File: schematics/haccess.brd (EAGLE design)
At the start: 86 x 86 mm, 30 parts, among them IC1 MCP2300X/SO, Q2 BSS123, X2 MICROMATCH-6-SMD

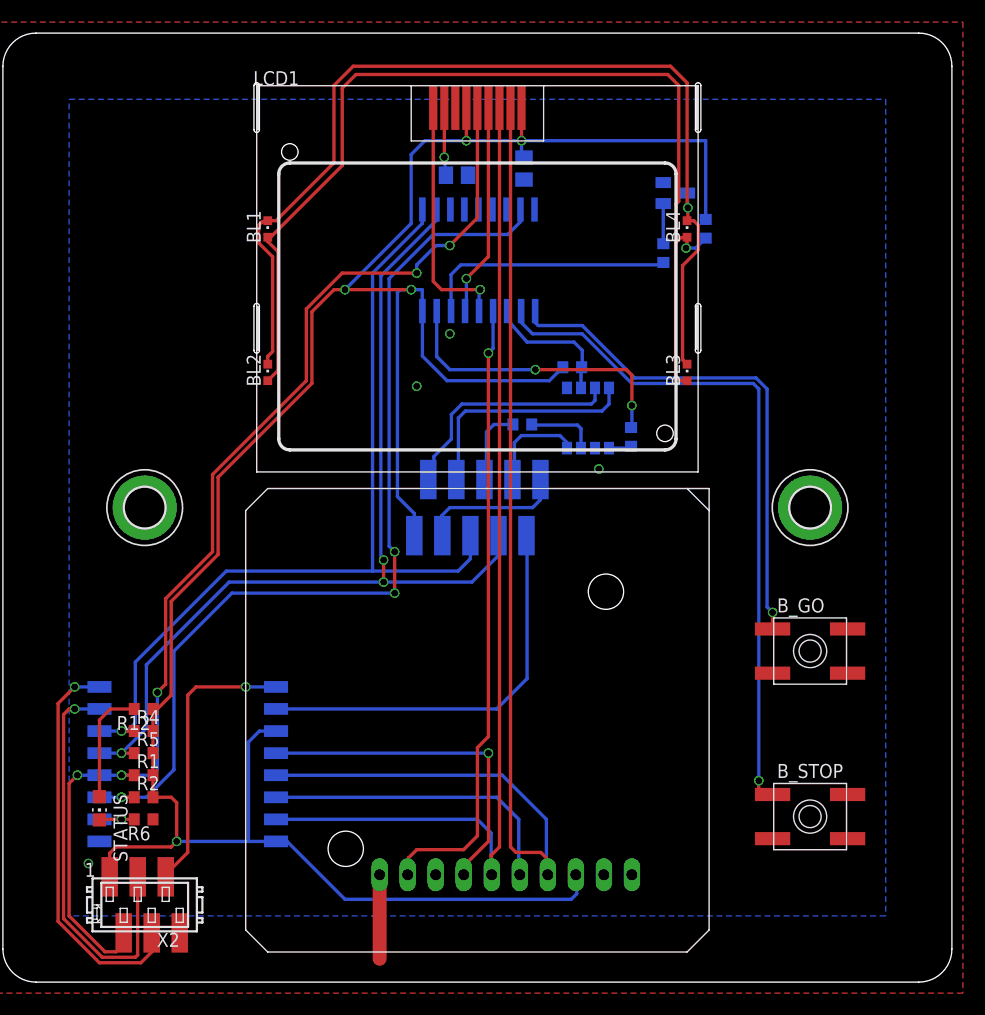
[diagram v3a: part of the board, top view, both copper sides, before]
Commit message: Added extra decoupling caps to ESP and MCP, added resistor to IRQ line, increased size of +3V3 lines, improved routing, fixed ground plane under ESP, changed switches to SKPMAPE010
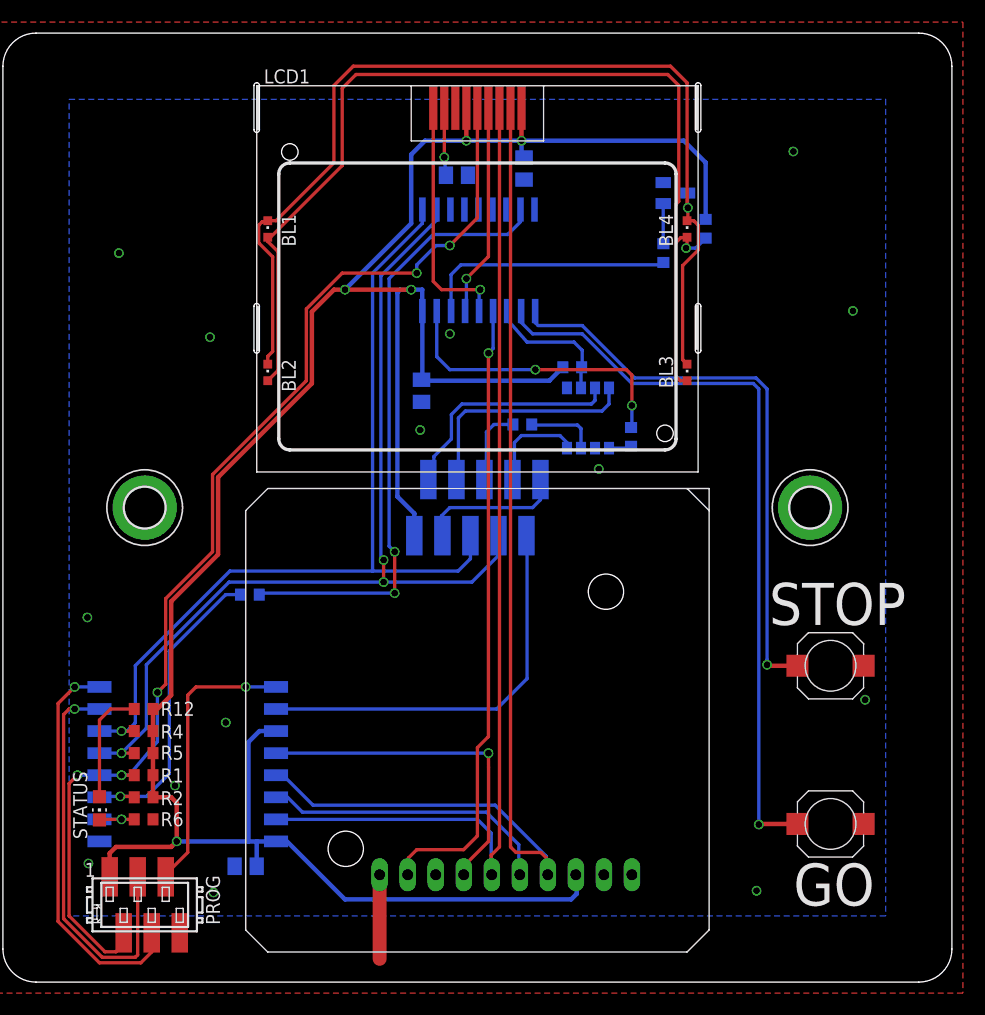
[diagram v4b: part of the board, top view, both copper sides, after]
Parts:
- removed B_GO, B_STOP: SPST_TACT-EVQQ2, adafruit:EVQ-Q2
- added C3, C4: 100nF, rcl:C0805K
- added R8: 22R, rcl:R0603
- added SW1, SW2: SPST_TACT, smtswitch:SKPMAPE010
- renumbered IC1 to U1, Q2 to Q1, U$2 to U2, U$3 to U3, X2 to PROG
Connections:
- new net !IRQ_1: R2.1, R8.2, U2.GPIO2
- net !IRQ: now also R8.1; no longer R2.1, U2.GPIO2
- net +3V3: now also C3.1, C4.1
- net GND: now also C3.2, C4.2, SW1.A, SW2.A; no longer B_GO.A, B_STOP.A
- net IN_G: now also SW2.B; no longer B_STOP.B
- net IN_R: now also SW1.B; no longer B_GO.B
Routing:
- net !IRQ: track 85.7 -> 56.2 mm, vias 3 -> 2
- net !IRQ_1: track 0.00 -> 28.2 mm, vias 0 -> 1
- net IN_R: track 46.5 -> 52.4 mm
- net IN_G: track 63.1 -> 68.1 mm
- net +3V3: track 228.7 -> 231.1 mm
- net SCK: track 103.4 -> 101.5 mm
- net MISO: track 27.9 -> 26.5 mm
- net CS0: track 105.9 -> 104.6 mm
- net GND: vias 4 -> 14
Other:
- board text added: "GO"
- board text added: "STOP"

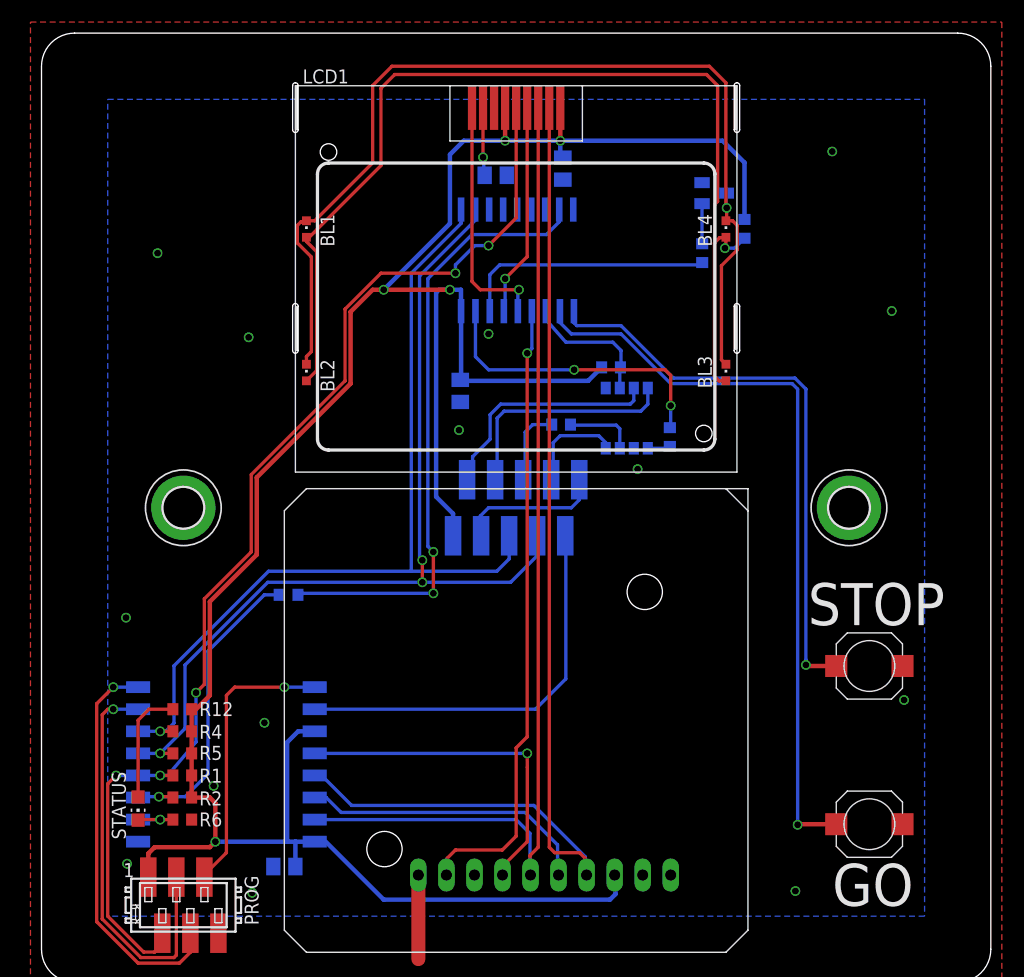
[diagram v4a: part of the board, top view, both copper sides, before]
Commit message: Added tant cap, increased size of 3V lines, improved documentation silks
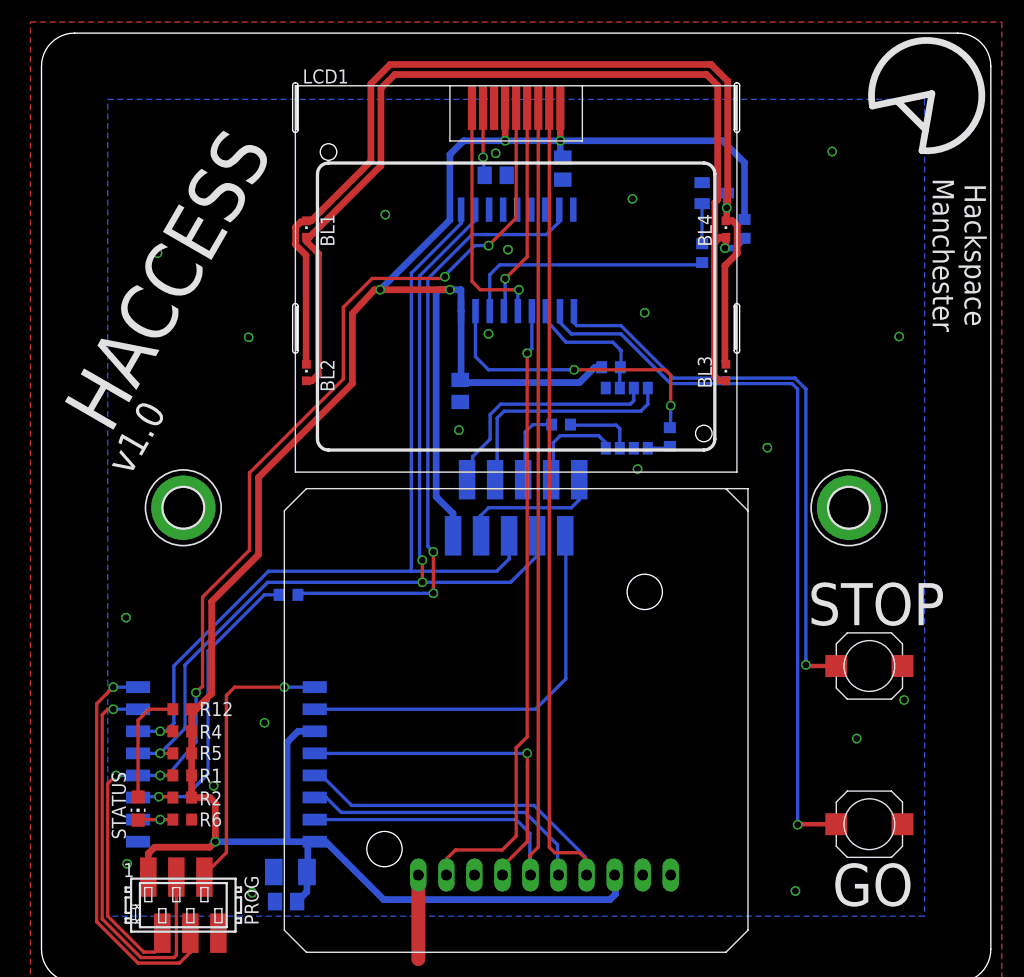
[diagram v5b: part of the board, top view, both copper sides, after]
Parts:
- added C5: (no value), rcl:SMC_B
- moved C3 3.18 mm to (22.2, 7.33)
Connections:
- net +3V3: now also C5.+
- net GND: now also C5.-
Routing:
- net +3V3: track 231.1 -> 234.8 mm
- net GND: vias 14 -> 21
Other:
- board text added: "+"
- board text added: "1"
- board text added: "HACCESS"
- board text added: "Hackspace Manchester"
- board text added: "v1.0"

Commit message: Board as purchased
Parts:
- moved C3 3.03 mm to (21.8, 10.3)
- moved C5 2.23 mm to (22.4, 7.78)
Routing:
- net GND: vias 21 -> 34
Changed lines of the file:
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@@
 <grid distance="0.15875" unitdist="mm" unit="mm" style="dots" multiple="1" display="yes" altdistance="0.025" altunitdist="inch" altunit="inch"/>
 <layers>
-<layer number="1" name="Top" color="4" fill="1" visible="no" active="yes"/>
+<layer number="1" name="Top" color="4" fill="1" visible="yes" active="yes"/>
 <layer number="16" name="Bottom" color="1" fill="1" visible="yes" active="yes"/>
 <layer number="17" name="Pads" color="2" fill="1" visible="yes" active="yes"/>
@@
 <attribute name="NAME" x="18.4" y="9.675" size="1.27" layer="25" rot="R270"/>
 </element>
-<element name="C3" library="rcl" package="C0805K" value="100nF" x="22.15875" y="7.325" smashed="yes" rot="MR0">
-<attribute name="NAME" x="20.30125" y="6.93" size="1.016" layer="26" rot="MR0"/>
+<element name="C3" library="rcl" package="C0805K" value="100nF" x="21.84125" y="10.34125" smashed="yes" rot="MR0">
+<attribute name="NAME" x="19.98375" y="9.94625" size="1.016" layer="26" rot="MR0"/>
 </element>
 <element name="C4" library="rcl" package="C0805K" value="100nF" x="37.93625" y="53.58625" smashed="yes" rot="MR270">
@@
 <element name="SW1" library="smtswitch" package="SKPMAPE010" value="SPST_TACT" x="75" y="28.666" rot="R180"/>
 <element name="SW2" library="smtswitch" package="SKPMAPE010" value="SPST_TACT" x="75" y="14.333" rot="R180"/>
-<element name="C5" library="rcl" package="SMC_B" value="" x="22.5425" y="10.00125" smashed="yes" rot="MR0">
-<attribute name="NAME" x="20.16125" y="9.68375" size="1.016" layer="26" rot="MR0"/>
-<attribute name="VALUE" x="24.4475" y="7.46125" size="1.016" layer="28" rot="MR0"/>
+<element name="C5" library="rcl" package="SMC_B" value="" x="22.38375" y="7.77875" smashed="yes" rot="MR0">
+<attribute name="NAME" x="20.0025" y="7.46125" size="1.016" layer="26" rot="MR0"/>
+<attribute name="VALUE" x="24.28875" y="5.23875" size="1.016" layer="28" rot="MR0"/>
 </element>
 </elements>
@@
 <via x="42.2625" y="66.3825" extent="1-16" drill="0.6"/>
 <via x="41.15125" y="75.11375" extent="1-16" drill="0.6"/>
+<via x="18.92625" y="15.74125" extent="1-16" drill="0.6"/>
+<via x="9.08375" y="72.25625" extent="1-16" drill="0.6"/>
+<via x="10.67125" y="54.3175" extent="1-16" drill="0.6"/>
+<via x="20.99" y="44.7925" extent="1-16" drill="0.6"/>
+<via x="6.54375" y="21.9325" extent="1-16" drill="0.6"/>
+<via x="17.18" y="10.5025" extent="1-16" drill="0.6"/>
+<via x="19.24375" y="19.71" extent="1-16" drill="0.6"/>
+<via x="20.51375" y="32.7275" extent="1-16" drill="0.6"/>
+<via x="47.81875" y="66.7" extent="1-16" drill="0.6"/>
+<via x="47.50125" y="63.36625" extent="1-16" drill="0.6"/>
+<via x="31.94375" y="60.35" extent="1-16" drill="0.6"/>
+<via x="54.645" y="50.5075" extent="1-16" drill="0.6"/>
+<via x="49.565" y="53.365" extent="1-16" drill="0.6"/>
 </signal>
 <signal name="+3V3" class="1">
@@
 <wire x1="14" y1="24.75" x2="15.40875" y2="26.15875" width="0.6096" layer="1"/>
 <wire x1="15.40875" y1="26.15875" x2="15.40875" y2="34.5" width="0.6096" layer="1"/>
-<wire x1="22.25" y1="12.75" x2="24.13" y2="12.75" width="0.6096" layer="16"/>
-<wire x1="24.13" y1="12.75" x2="24.75" y2="12.75" width="0.6096" layer="16"/>
+<wire x1="22.25" y1="12.75" x2="22.86" y2="12.75" width="0.6096" layer="16"/>
+<wire x1="22.86" y1="12.75" x2="24.75" y2="12.75" width="0.6096" layer="16"/>
 <wire x1="22.25" y1="12.75" x2="15.75" y2="12.75" width="0.6096" layer="16"/>
 <via x="15.75" y="12.75" extent="1-16" drill="0.6"/>
@@
 <wire x1="50.11625" y1="55.72125" x2="48.73625" y2="54.34125" width="0.6096" layer="16"/>
 <contactref element="C5" pad="+"/>
-<wire x1="23.15875" y1="7.325" x2="24.0425" y2="8.20875" width="0.6096" layer="16"/>
-<wire x1="24.0425" y1="8.20875" x2="24.0425" y2="10.00125" width="0.6096" layer="16"/>
-<wire x1="24.0425" y1="10.00125" x2="24.13" y2="10.40625" width="0.6096" layer="16"/>
-<wire x1="24.13" y1="10.40625" x2="24.13" y2="12.75" width="0.6096" layer="16"/>
+<wire x1="23.88375" y1="7.77875" x2="22.84125" y2="8.82125" width="0.6096" layer="16"/>
+<wire x1="22.84125" y1="8.82125" x2="22.84125" y2="10.34125" width="0.6096" layer="16"/>
+<wire x1="22.84125" y1="10.34125" x2="22.86" y2="10.36" width="0.6096" layer="16"/>
+<wire x1="22.86" y1="10.36" x2="22.86" y2="12.75" width="0.6096" layer="16"/>
 </signal>
 <signal name="N$1">
@@
 <wire x1="24" y1="69" x2="24.4325" y2="69" width="0.6096" layer="1"/>
 <wire x1="24.4325" y1="69" x2="29.84125" y2="74.40875" width="0.6096" layer="1"/>
-<wire x1="29.84125" y1="74.40875" x2="29.84125" y2="81.40875" width="0.6096" layer="1"/>
-<wire x1="29.84125" y1="81.40875" x2="31.59125" y2="83.15875" width="0.6096" layer="1"/>
-<wire x1="31.59125" y1="83.15875" x2="60.65875" y2="83.15875" width="0.6096" layer="1"/>
-<wire x1="60.65875" y1="83.15875" x2="62.15875" y2="81.65875" width="0.6096" layer="1"/>
-<wire x1="62.15875" y1="81.65875" x2="62.15875" y2="70.23875" width="0.6096" layer="1"/>
+<wire x1="29.84125" y1="74.40875" x2="29.84125" y2="81.5675" width="0.6096" layer="1"/>
+<wire x1="29.84125" y1="81.5675" x2="31.59125" y2="83.3175" width="0.6096" layer="1"/>
+<wire x1="31.59125" y1="83.3175" x2="60.65875" y2="83.3175" width="0.6096" layer="1"/>
+<wire x1="60.65875" y1="83.3175" x2="62.15875" y2="81.8175" width="0.6096" layer="1"/>
+<wire x1="62.15875" y1="81.8175" x2="62.15875" y2="70.23875" width="0.6096" layer="1"/>
 <wire x1="62.15875" y1="70.23875" x2="62.07125" y2="70.1675" width="0.6096" layer="1"/>
 </signal>
@@
 <wire x1="24" y1="67.5" x2="24.25" y2="67.5" width="0.6096" layer="1"/>
 <wire x1="24.25" y1="67.5" x2="30.75" y2="74" width="0.6096" layer="1"/>
-<wire x1="30.75" y1="74" x2="30.75" y2="81" width="0.6096" layer="1"/>
-<wire x1="30.75" y1="81" x2="32" y2="82.25" width="0.6096" layer="1"/>
-<wire x1="32" y1="82.25" x2="60.25" y2="82.25" width="0.6096" layer="1"/>
-<wire x1="60.25" y1="82.25" x2="61.25" y2="81.25" width="0.6096" layer="1"/>
-<wire x1="61.25" y1="81.25" x2="61.25" y2="70.90875" width="0.6096" layer="1"/>
+<wire x1="30.75" y1="74" x2="30.75" y2="81.15875" width="0.6096" layer="1"/>
+<wire x1="30.75" y1="81.15875" x2="32" y2="82.40875" width="0.6096" layer="1"/>
+<wire x1="32" y1="82.40875" x2="60.25" y2="82.40875" width="0.6096" layer="1"/>
+<wire x1="60.25" y1="82.40875" x2="61.25" y2="81.40875" width="0.6096" layer="1"/>
+<wire x1="61.25" y1="81.40875" x2="61.25" y2="70.90875" width="0.6096" layer="1"/>
 <wire x1="61.25" y1="70.90875" x2="61" y2="70.65875" width="0.6096" layer="1"/>
 <wire x1="61" y1="70.65875" x2="61" y2="67.0325" width="0.6096" layer="1"/>

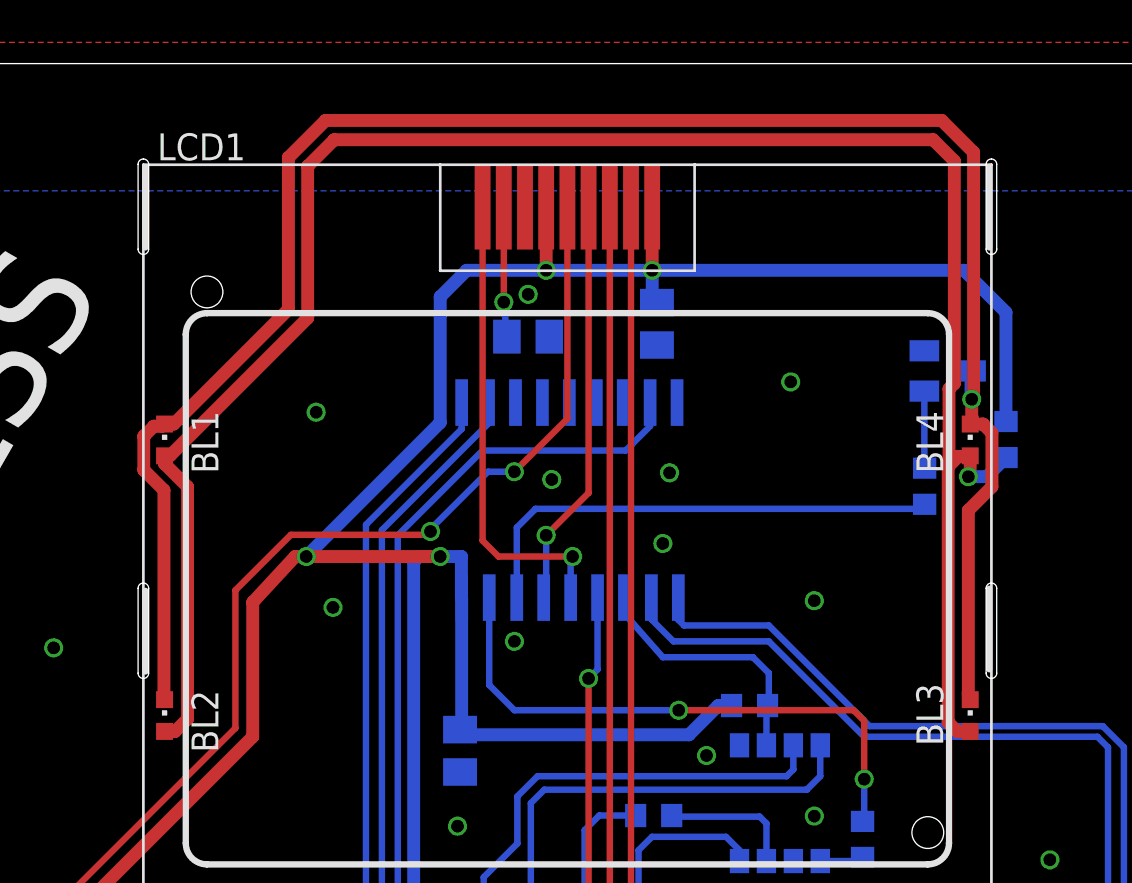
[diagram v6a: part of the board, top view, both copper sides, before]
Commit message: Changed backlight to use 0805 pads - still usable with 0603 parts, but easier to solder
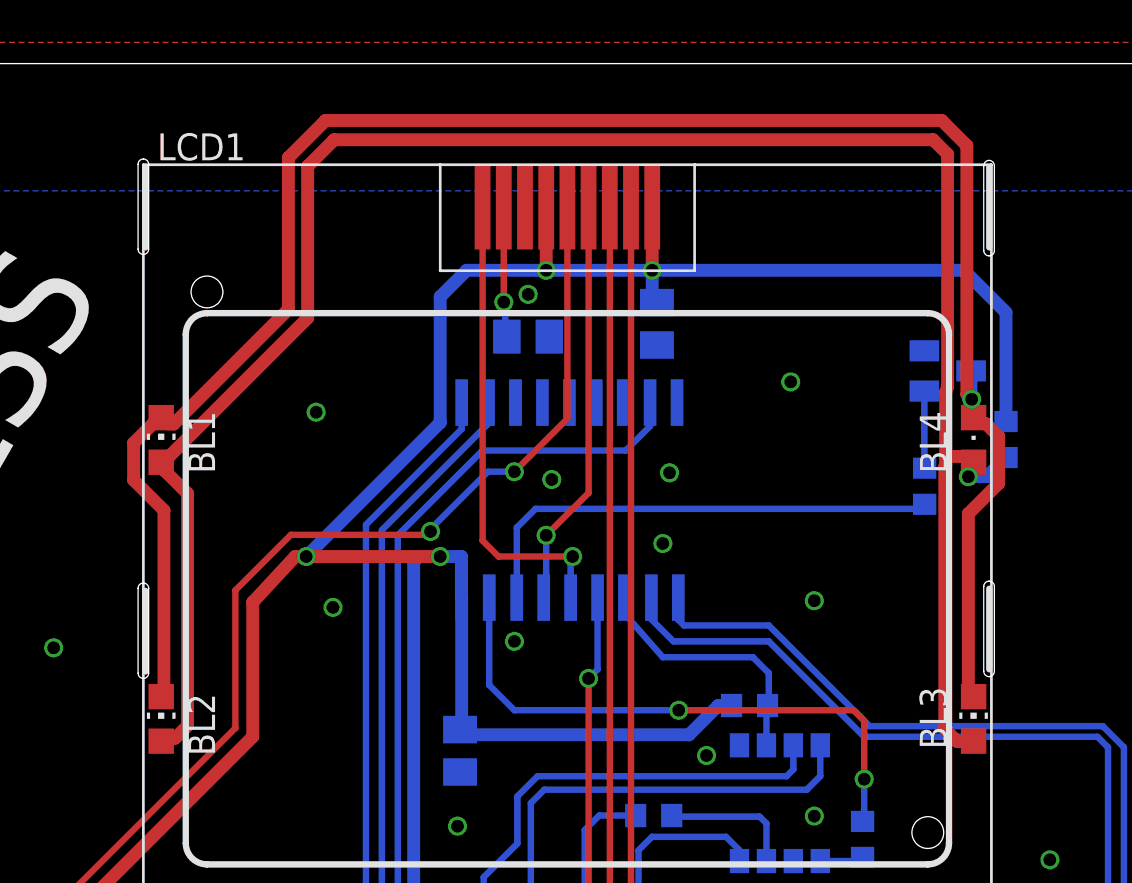
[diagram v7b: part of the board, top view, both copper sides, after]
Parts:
- BL1, BL2, BL3: device led:CHIPLED_0603 -> led:CHIP-LED0805
- BL4: device led:CHIPLED_0603 -> led:CHIPLED_0805
- moved BL2 0.22 mm to (23.8, 55.1)
- moved BL3 0.22 mm to (62.2, 55.1)
- moved BL1 0.16 mm to (23.8, 68.2)
- moved BL4 0.16 mm to (62.2, 68.2)
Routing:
- net N$18: track 91.6 -> 93.1 mm
- net N$19: track 94.4 -> 95.3 mm
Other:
- outline, holes or cut-outs redrawn
